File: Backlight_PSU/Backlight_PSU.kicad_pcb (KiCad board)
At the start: 2 copper layers, 28 x 35 mm, 15 parts, among them J1 Conn_01x01, J2 Conn_01x01, J3 Conn_01x01, J4 Conn_01x01, U1 NCP1117-ADJ_SOT223

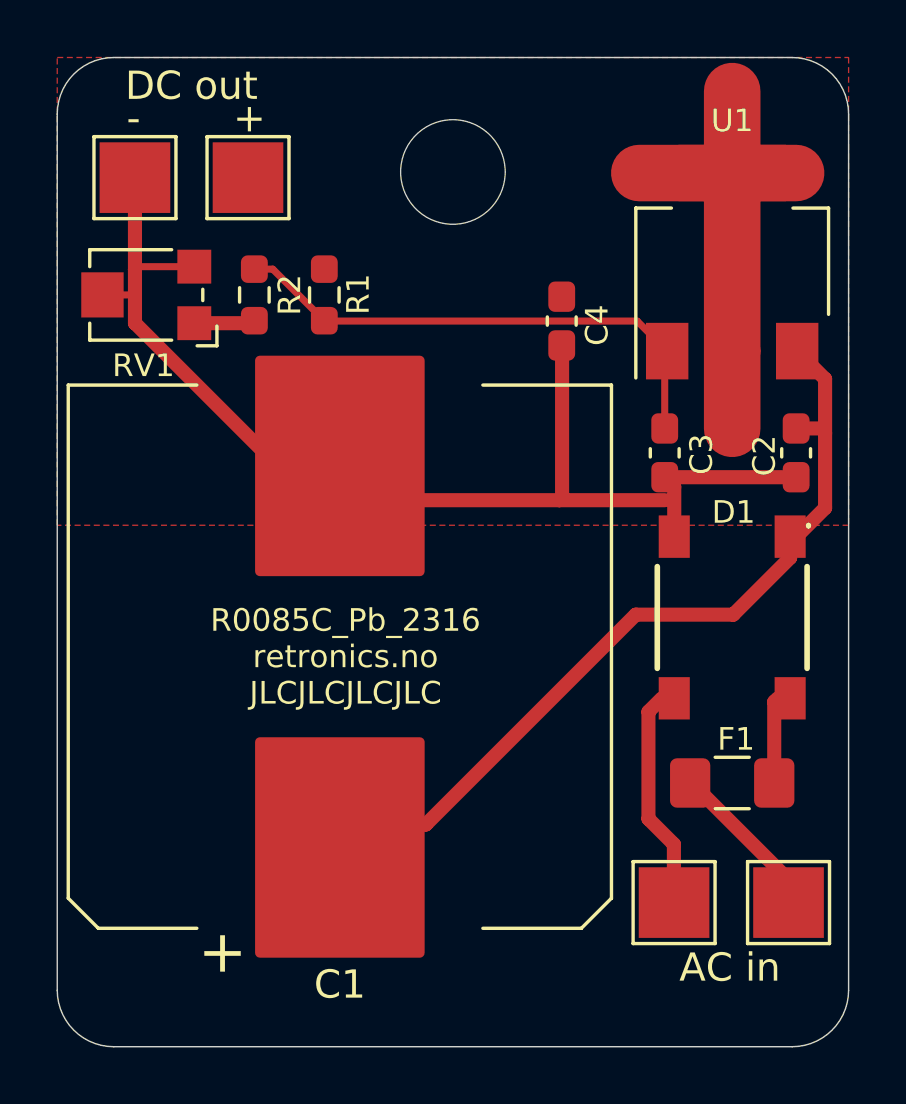
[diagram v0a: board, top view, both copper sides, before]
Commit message: Changed capacitor footprint
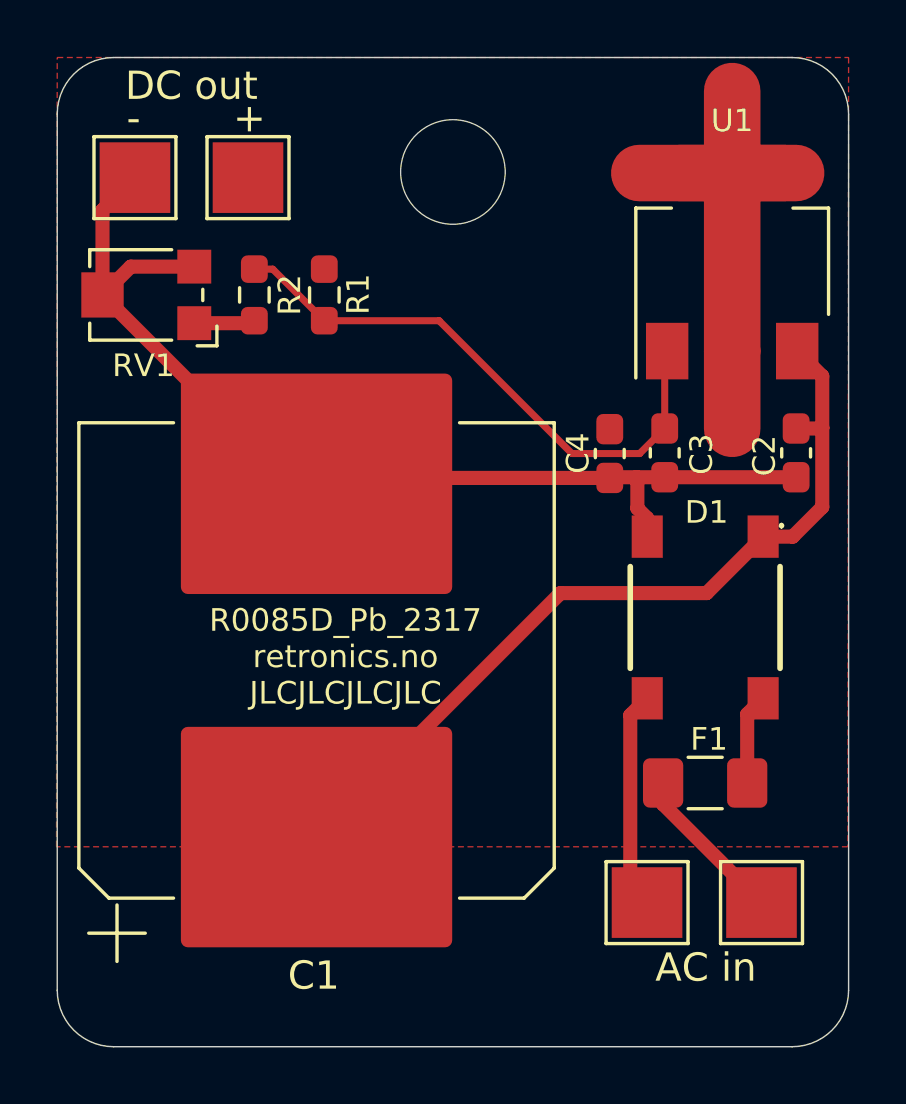
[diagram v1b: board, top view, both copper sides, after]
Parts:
- C1: value 4700µF 16V -> 2200µF 25V; footprint Capacitor_SMD:CP_Elec_18x17.5 -> Capacitor_SMD:CP_Elec_16x17.5
- moved C4 4.99 mm to (171.6, 110.0)
- moved J1 0.96 mm to (176.9, 125.9)
- moved D1 0.96 mm to (174.9, 115.8)
- moved F1 0.96 mm to (174.9, 121.7)
- moved J3 0.96 mm to (172.9, 125.9)
- moved C1 0.84 mm to (161.2, 117.3)
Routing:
- net Net-(D1--): track 42.1 -> 38.0 mm
- net Net-(U1-ADJ): track 18.6 -> 20.4 mm
- net Net-(J1-Pin_1): track 4.89 -> 5.67 mm
- net Net-(J3-Pin_1): track 6.98 -> 7.72 mm
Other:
- board text added: "R0085D_Pb_2317 retronics.no JLCJLCJLCJLC"
- board text removed: "R0085C_Pb_2316 retronics.no JLCJLCJLCJLC"

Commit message: Minor silkscreen update
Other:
- board text added: "."
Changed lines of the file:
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@@
     (fp_line (start 1.6 0.8) (end -1.6 0.8)
       (stroke (width 0.1) (type solid)) (layer "F.Fab"))
-    (pad "1" smd roundrect (at -1.4875 0 180) (size 1.425 1.75) (layers "F.Cu" "F.Paste" "F.Mask") (roundrect_rratio 0.1754385965)
+    (pad "1" smd roundrect (at -1.4875 0 180) (size 1.425 1.75) (layers "F.Cu" "F.Paste" "F.Mask") (roundrect_rratio 0.175439)
       (net 5 "Net-(D1-Pad2)") (pintype "passive"))
-    (pad "2" smd roundrect (at 1.4875 0 180) (size 1.425 1.75) (layers "F.Cu" "F.Paste" "F.Mask") (roundrect_rratio 0.1754385965)
+    (pad "2" smd roundrect (at 1.4875 0 180) (size 1.425 1.75) (layers "F.Cu" "F.Paste" "F.Mask") (roundrect_rratio 0.175439)
       (net 7 "Net-(J1-Pin_1)") (pintype "passive"))
-    (model "${KISYS3DMOD}/Fuse.3dshapes/Fuse_1206_3216Metric.wrl"
+    (model "${KICAD6_3DMODEL_DIR}/Fuse.3dshapes/Fuse_1206_3216Metric.wrl"
       (offset (xyz 0 0 0))
       (scale (xyz 1 1 1))
@@
     (property "ki_description" "Mounting Hole without connection")
     (property "ki_keywords" "mounting hole")
-    (clearance 2.1)
     (attr exclude_from_pos_files)
     (fp_text reference "H1" (at 0 -4.7) (layer "F.SilkS") hide
@@
     (fp_line (start 2.65 -1.8) (end 2.65 1.8)
       (stroke (width 0.2) (type solid)) (layer "F.SilkS"))
-    (fp_line (start 2.7 -3.2) (end 2.7 -3.3)
-      (stroke (width 0.1) (type solid)) (layer "F.SilkS"))
-    (fp_line (start 2.7 -3.2) (end 2.7 -3.2)
-      (stroke (width 0.1) (type solid)) (layer "F.SilkS"))
-    (fp_arc (start 2.7 -3.3) (mid 2.75 -3.25) (end 2.7 -3.2)
-      (stroke (width 0.1) (type solid)) (layer "F.SilkS"))
-    (fp_arc (start 2.7 -3.2) (mid 2.65 -3.25) (end 2.7 -3.3)
-      (stroke (width 0.1) (type solid)) (layer "F.SilkS"))
     (fp_line (start -3 -3.75) (end 3 -3.75)
       (stroke (width 0.1) (type solid)) (layer "F.CrtYd"))
@@
     (effects (font (size 1 1) (thickness 0.15)))
   )
+  (gr_text "." (at 177.85 113.175) (layer "F.SilkS")
+    (effects (font (size 1.5 1.5) (thickness 0.3) bold) (justify left bottom))
+  )
   (segment (start 178.14375 110.85) (end 173.49375 110.85) (width 0.5) (layer "F.Cu") (net 1))

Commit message: Changed fill zone
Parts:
- RV1: footprint Potentiometer_SMD:Potentiometer_TT_35W -> Potentiometer_SMD:Potentiometer_Bourns_TC33X_Vertical
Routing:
- net Net-(J2-Pin_1): track 23.8 -> 0.00 mm
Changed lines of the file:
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@@
   (net 6 "Net-(J3-Pin_1)")
   (net 7 "Net-(J1-Pin_1)")
-  (net 8 "Net-(D1-+)")
+  (net 8 "Net-(#FLG01-pwr)")
   (footprint "Capacitor_SMD:CP_Elec_16x17.5" (layer "F.Cu")
     (at 161.175 117.3325 90)
@@
     (fp_circle (center 0 0) (end 8 0)
       (stroke (width 0.1) (type solid)) (fill none) (layer "F.Fab"))
-    (pad "1" smd roundrect (at -6.25 0 90) (size 7.8 9.6) (layers "F.Cu" "F.Paste" "F.Mask") (roundrect_rratio 0.032051)
-      (net 8 "Net-(D1-+)") (pintype "passive"))
-    (pad "2" smd roundrect (at 6.25 0 90) (size 7.8 9.6) (layers "F.Cu" "F.Paste" "F.Mask") (roundrect_rratio 0.032051)
+    (pad "1" smd roundrect (at -6.25 0 90) (size 7.8 9.6) (layers "F.Cu" "F.Paste" "F.Mask") (roundrect_rratio 0.03205102564)
+      (net 8 "Net-(#FLG01-pwr)") (pintype "passive"))
+    (pad "2" smd roundrect (at 6.25 0 90) (size 7.8 9.6) (layers "F.Cu" "F.Paste" "F.Mask") (roundrect_rratio 0.03205102564)
       (net 1 "Net-(D1--)") (pintype "passive"))
     (model "${KICAD6_3DMODEL_DIR}/Capacitor_SMD.3dshapes/CP_Elec_16x17.5.wrl"
@@
     (fp_line (start 1.6 0.8) (end -1.6 0.8)
       (stroke (width 0.1) (type solid)) (layer "F.Fab"))
-    (pad "1" smd roundrect (at -1.4875 0 180) (size 1.425 1.75) (layers "F.Cu" "F.Paste" "F.Mask") (roundrect_rratio 0.175439)
+    (pad "1" smd roundrect (at -1.4875 0 180) (size 1.425 1.75) (layers "F.Cu" "F.Paste" "F.Mask") (roundrect_rratio 0.1754392982)
       (net 5 "Net-(D1-Pad2)") (pintype "passive"))
-    (pad "2" smd roundrect (at 1.4875 0 180) (size 1.425 1.75) (layers "F.Cu" "F.Paste" "F.Mask") (roundrect_rratio 0.175439)
+    (pad "2" smd roundrect (at 1.4875 0 180) (size 1.425 1.75) (layers "F.Cu" "F.Paste" "F.Mask") (roundrect_rratio 0.1754392982)
       (net 7 "Net-(J1-Pin_1)") (pintype "passive"))
     (model "${KICAD6_3DMODEL_DIR}/Fuse.3dshapes/Fuse_1206_3216Metric.wrl"
@@
     (property "ki_description" "Mounting Hole without connection")
     (property "ki_keywords" "mounting hole")
+    (clearance 2.2)
     (attr exclude_from_pos_files)
     (fp_text reference "H1" (at 0 -4.7) (layer "F.SilkS") hide
@@
     (fp_line (start 2.65 -1.8) (end 2.65 1.8)
       (stroke (width 0.2) (type solid)) (layer "F.SilkS"))
+    (fp_line (start 2.7 -3.2) (end 2.7 -3.3)
+      (stroke (width 0.1) (type solid)) (layer "F.SilkS"))
+    (fp_line (start 2.7 -3.2) (end 2.7 -3.2)
+      (stroke (width 0.1) (type solid)) (layer "F.SilkS"))
+    (fp_arc (start 2.7 -3.3) (mid 2.75 -3.25) (end 2.7 -3.2)
+      (stroke (width 0.1) (type solid)) (layer "F.SilkS"))
+    (fp_arc (start 2.7 -3.2) (mid 2.65 -3.25) (end 2.7 -3.3)
+      (stroke (width 0.1) (type solid)) (layer "F.SilkS"))
     (fp_line (start -3 -3.75) (end 3 -3.75)
       (stroke (width 0.1) (type solid)) (layer "F.CrtYd"))
@@
       (stroke (width 0.1) (type solid)) (layer "F.Fab"))
     (pad "1" smd rect (at 2.05 -2.86) (size 1.1 1.5) (layers "F.Cu" "F.Paste" "F.Mask")
-      (net 8 "Net-(D1-+)") (pinfunction "+") (pintype "passive"))
+      (net 8 "Net-(#FLG01-pwr)") (pinfunction "+") (pintype "passive"))
     (pad "2" smd rect (at 2.05 2.86) (size 1.1 1.5) (layers "F.Cu" "F.Paste" "F.Mask")
       (net 5 "Net-(D1-Pad2)") (pintype "passive"))
@@
       (stroke (width 0.1) (type solid)) (layer "F.Fab"))
     (pad "1" smd roundrect (at -0.8625 0 270) (size 1.075 0.95) (layers "F.Cu" "F.Paste" "F.Mask") (roundrect_rratio 0.25)
-      (net 8 "Net-(D1-+)") (pintype "passive"))
+      (net 8 "Net-(#FLG01-pwr)") (pintype "passive"))
     (pad "2" smd roundrect (at 0.8625 0 270) (size 1.075 0.95) (layers "F.Cu" "F.Paste" "F.Mask") (roundrect_rratio 0.25)
       (net 1 "Net-(D1--)") (pintype "passive"))
@@
       (net 4 "Net-(J2-Pin_1)") (pinfunction "Pin_1") (pintype "passive"))
   )
-  (footprint "Potentiometer_SMD:Potentiometer_TT_35W" (layer "F.Cu")
+  (footprint "Potentiometer_SMD:Potentiometer_Bourns_TC33X_Vertical" (layer "F.Cu")
     (at 155.05 104.4 180)
     (descr "Potentiometer, Bourns, TC33X, Vertical, https://www.bourns.com/pdfs/TC33.pdf")
     (tags "Potentiometer Bourns TC33X Vertical")
+    (property "Comments" "")
     (property "Sheetfile" "Backlight_PSU.kicad_sch")
     (property "Sheetname" "")
@@
     (attr smd)
     (fp_text reference "RV1" (at 0 -2.5 180) (layer "F.SilkS")
-        (effects (font (size 0.8 0.8) (thickness 0.1)))
-    )
-    (fp_text value "500Ω" (at 0 2.5) (layer "F.Fab")
-        (effects (font (size 1 1) (thickness 0.15)))
-    )
-    (fp_text user "Wiper may be\nanywhere within\ncircle shown" (at -0.15 -0.8) (layer "Cmts.User")
+        (effects (font (size 1 1) (thickness 0.15)))
+    )
+    (fp_text value "500Ω" (at 0 2.5 180) (layer "F.Fab")
+        (effects (font (size 1 1) (thickness 0.15)))
+    )
+    (fp_text user "Wiper may be\nanywhere within\ncircle shown" (at -0.15 -0.8 180) (layer "Cmts.User")
         (effects (font (size 0.15 0.15) (thickness 0.02)))
     )
-    (fp_text user "${REFERENCE}" (at 0 0) (layer "F.Fab")
+    (fp_text user "${REFERENCE}" (at 0 0 180) (layer "F.Fab")
         (effects (font (size 0.7 0.7) (thickness 0.105)))
     )
@@
     (pad "3" smd rect (at -1.8 1 180) (size 1.2 1.2) (layers "F.Cu" "F.Paste" "F.Mask")
       (net 1 "Net-(D1--)") (pinfunction "3") (pintype "passive"))
-    (model "${KICAD6_3RD_PARTY}/myDevices.3dshapes/35W.stp"
-      (offset (xyz -0.1 0 0))
-      (scale (xyz 1 1 1))
-      (rotate (xyz -90 0 90))
+    (model "${KICAD6_3DMODEL_DIR}/Potentiometer_SMD.3dshapes/Potentiometer_Bourns_TC33X_Vertical.wrl"
+      (offset (xyz 0 0 0))
+      (scale (xyz 1 1 1))
+      (rotate (xyz 0 0 0))
     )
   )
@@
       (net 4 "Net-(J2-Pin_1)") (pinfunction "VO") (pintype "power_out"))
     (pad "3" smd rect (at -3.15 2.3 90) (size 2 1.5) (layers "F.Cu" "F.Paste" "F.Mask")
-      (net 8 "Net-(D1-+)") (pinfunction "VI") (pintype "power_in"))
+      (net 8 "Net-(#FLG01-pwr)") (pinfunction "VI") (pintype "power_in"))
     (model "${KICAD6_3DMODEL_DIR}/Package_TO_SOT_SMD.3dshapes/SOT-223.wrl"
       (offset (xyz 0 0 0))
@@
   (segment (start 173.49375 106.475) (end 173.58125 106.3875) (width 0.5) (layer "F.Cu") (net 3))
   (segment (start 173.49375 109.125) (end 173.49375 106.475) (width 0.25) (layer "F.Cu") (net 3))
-  (segment (start 175.24375 100.0875) (end 172.59375 100.0875) (width 2) (layer "F.Cu") (net 4))
-  (segment (start 175.88125 106.3875) (end 175.88125 97.1875) (width 2) (layer "F.Cu") (net 4))
-  (segment (start 175.24375 100.0875) (end 178.14375 100.0875) (width 2) (layer "F.Cu") (net 4))
-  (segment (start 175.88125 106.3875) (end 175.88125 109.1375) (width 2) (layer "F.Cu") (net 4))
-  (segment (start 175.24375 106.3875) (end 175.24375 100.0875) (width 0.5) (layer "F.Cu") (net 4))
   (segment (start 176.4125 119.235) (end 176.975 118.6725) (width 0.5) (layer "F.Cu") (net 5))
   (segment (start 176.4125 121.66875) (end 176.4125 119.235) (width 0.5) (layer "F.Cu") (net 5))
@@
   (segment (start 178.14375 109.125) (end 179.04375 109.125) (width 0.5) (layer "F.Cu") (net 8))
   (segment (start 179.06875 109.1) (end 179.06875 107.275) (width 0.5) (layer "F.Cu") (net 8))
+  (zone (net 4) (net_name "Net-(J2-Pin_1)") (layer "F.Cu") (hatch edge 0.5)
+    (priority 1)
+    (connect_pads yes (clearance 0.254))
+    (min_thickness 0.25) (filled_areas_thickness no)
+    (fill yes (thermal_gap 0.5) (thermal_bridge_width 0.5))
+    (polygon
+      (pts
+        (xy 172.25 98.5)
+        (xy 179.5 98.5)
+        (xy 179.5 105.5)
+        (xy 172.25 105.5)
+      )
+    )
+  )
   (zone (net 4) (net_name "Net-(J2-Pin_1)") (layer "F.Cu") (hatch edge 0.508)
     (connect_pads (clearance 0.254))
